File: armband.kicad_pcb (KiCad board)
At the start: 6 copper layers, 151.9 x 110.6 mm, 86 parts, among them IC1 QSMP-1570, IC10 TLE493DW2B6A0HTSA1, IC2 BMI323, IC3 TPS259571DSGR, IC4 TPD6E001RSERG4, IC5 MP2722GRH-0000-Z, IC6 TPS62291DRVR, IC7 TPS62293DRVR, IC8 BQ27427YZFR, IC9 nRF52832-CIAA-G-R7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

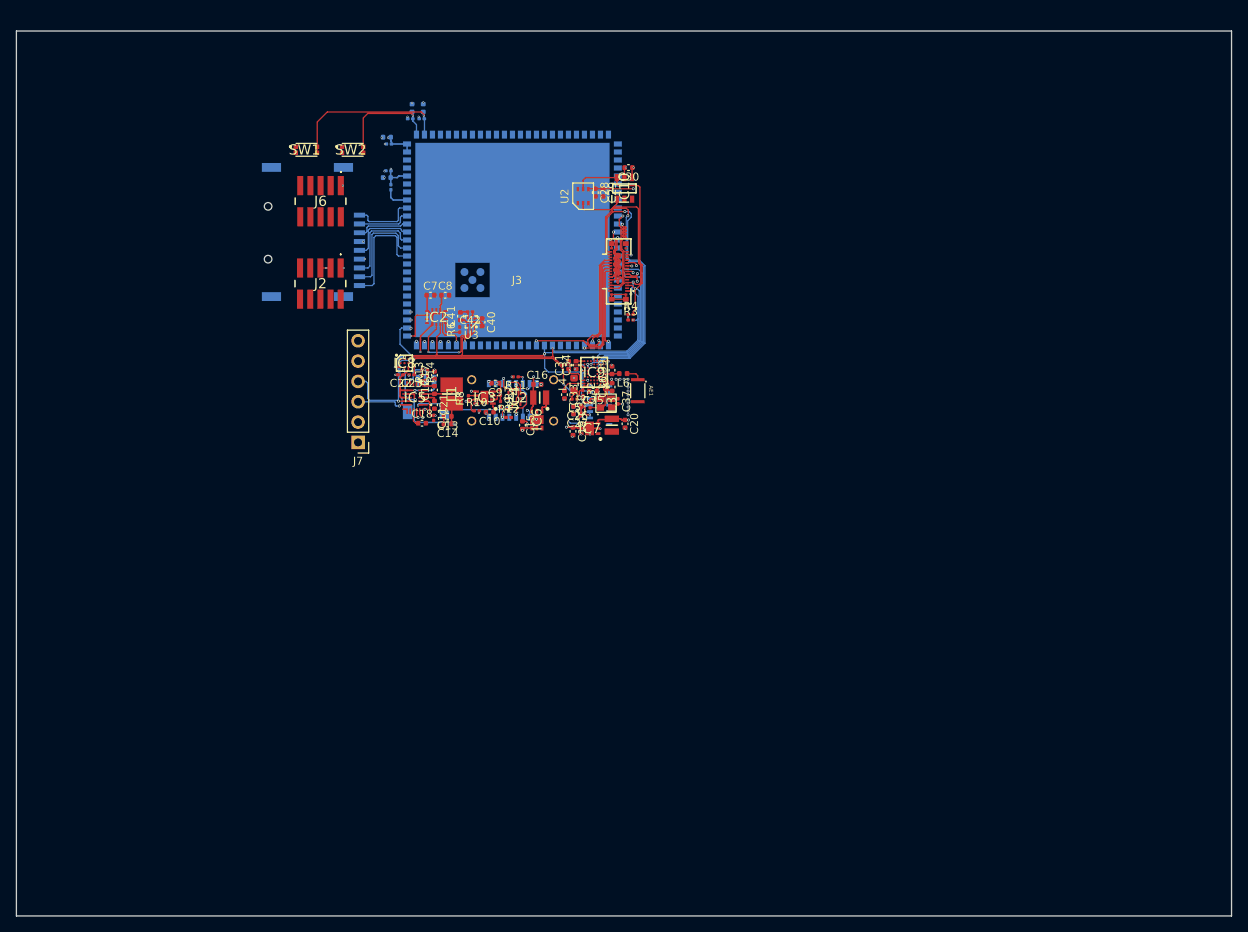
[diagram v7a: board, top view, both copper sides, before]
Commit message: added edge.cuts
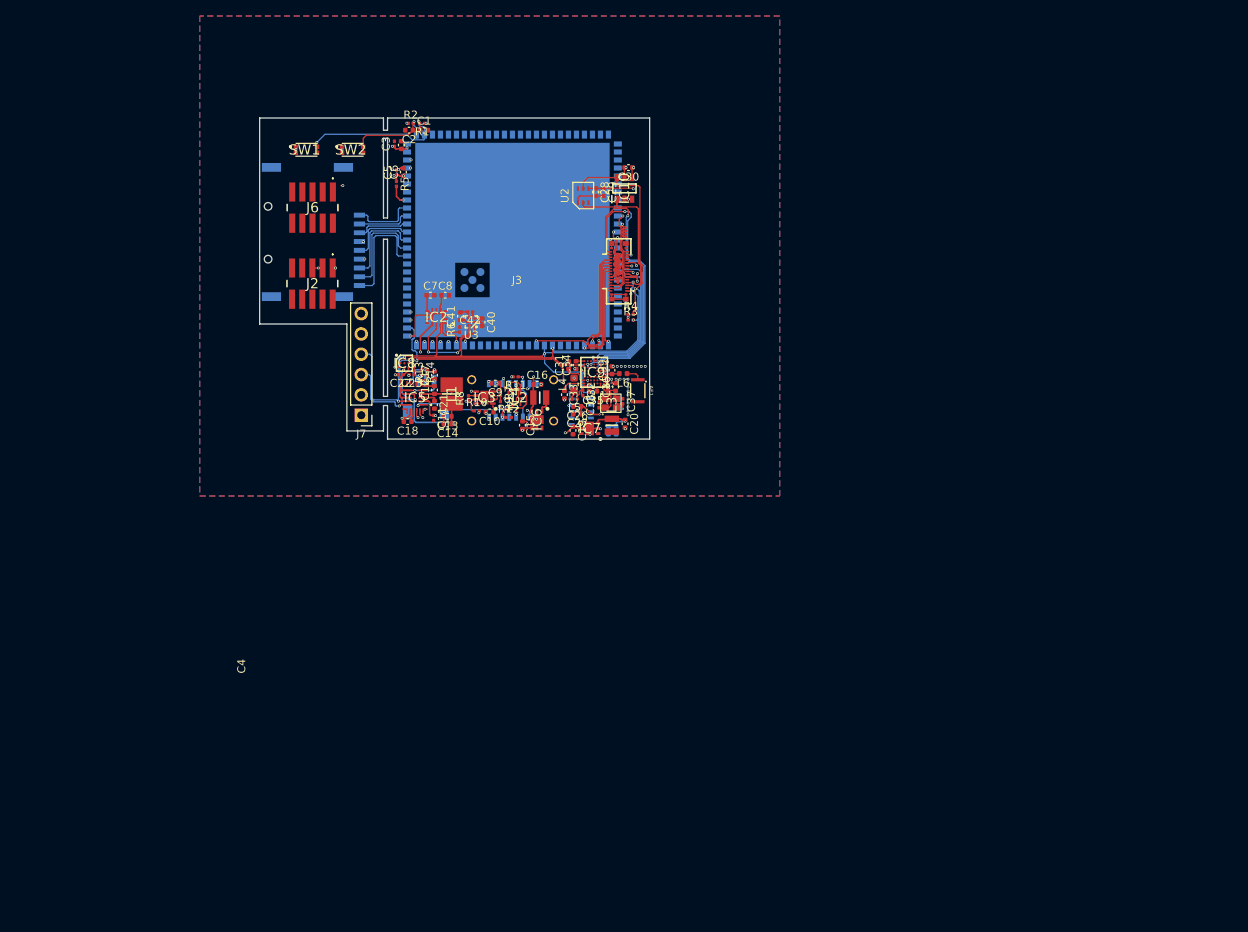
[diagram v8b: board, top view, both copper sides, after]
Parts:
- C1, C2, C3, C4, C5, C6, R1, R2, R5: moved to F.Cu
- moved C24 5.27 mm to (154.6, 86.8), turned to -90 degrees
- moved C25 4.92 mm to (153.6, 86.8), turned to -90 degrees
- moved J7 3.42 mm to (122.7, 84.9)
- moved C2 2.80 mm to (128.7, 49.3), turned to 180 degrees
- moved C1 2.78 mm to (130.6, 49.3), turned to 0 degrees
- moved U1 2.30 mm to (150.2, 83.7)
- moved C6 2.18 mm to (128.0, 54.5), turned to 90 degrees
- moved C4 2.06 mm to (127.7, 51.1), turned to 90 degrees
- moved C18 1.81 mm to (128.5, 85.7), turned to 180 degrees
- moved J6 1.28 mm to (116.6, 59.0)
- moved C38 1.10 mm to (152.4, 83.6)
- moved C5 1.02 mm to (127.1, 54.6), turned to 90 degrees
- moved J2 1.00 mm to (116.6, 68.5)
- moved R5 0.82 mm to (127.1, 56.0)
- moved C3 0.69 mm to (126.8, 51.0), turned to 90 degrees
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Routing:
- net +1V8: track 21.7 -> 28.8 mm, vias 4 -> 5
- net GND: track 26.9 -> 33.1 mm, vias 53 -> 58
- net MAX_INT: track 28.6 -> 31.7 mm
- net QSMP_VBUS: track 53.0 -> 50.3 mm, vias 3 -> 4
- net QSMP_SCL: track 97.7 -> 100.4 mm
- net QSMP_SDA: track 100.3 -> 102.8 mm
- net QSMP_NRST: track 14.1 -> 11.7 mm
- net QSMP_BUCK_1V8_EN: track 2.13 -> 0.50 mm, vias 2 -> 1
- net QSMP_BOOT: track 20.9 -> 19.7 mm, vias 1 -> 2
- net +3V3: track 29.1 -> 29.9 mm, vias 15 -> 16
- net QSMP_USB_DP: track 3.98 -> 4.49 mm, vias 2 -> 3
- net Net-(IC5-VCC): track 1.94 -> 1.43 mm
- net QSMP_USB_DN: track 8.15 -> 8.60 mm, vias 3 -> 4
- net NRF_SWCLK: track 0.00 -> 0.41 mm, vias 0 -> 1
- net Net-(IC1-USBA_VBUS): track 3.13 -> 2.76 mm, vias 0 -> 1
- added copper zone on In4.Cu, net +3V3
- added copper zone on B.Cu, net GND
- added copper zone on F.Cu, net GND
- added copper zone on In1.Cu, net GND
- added copper zone on In2.Cu, net GND
- added copper zone on In3.Cu, net GND
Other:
- board size 151.9 x 110.6 mm -> 48.8 x 40.1 mm
